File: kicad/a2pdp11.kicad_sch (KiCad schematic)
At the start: 21 parts, among them SW1 HALT, SW2 INIT, U1 74LS07, U2 DCJ11, U3 SN74LVC245AN, U4 SN74LVC245AN, U5 SN74LVC245AN, U6 SN74LVC245AN, U7 TangNano9K, U8 SN74LVC245AN, Y1 18M

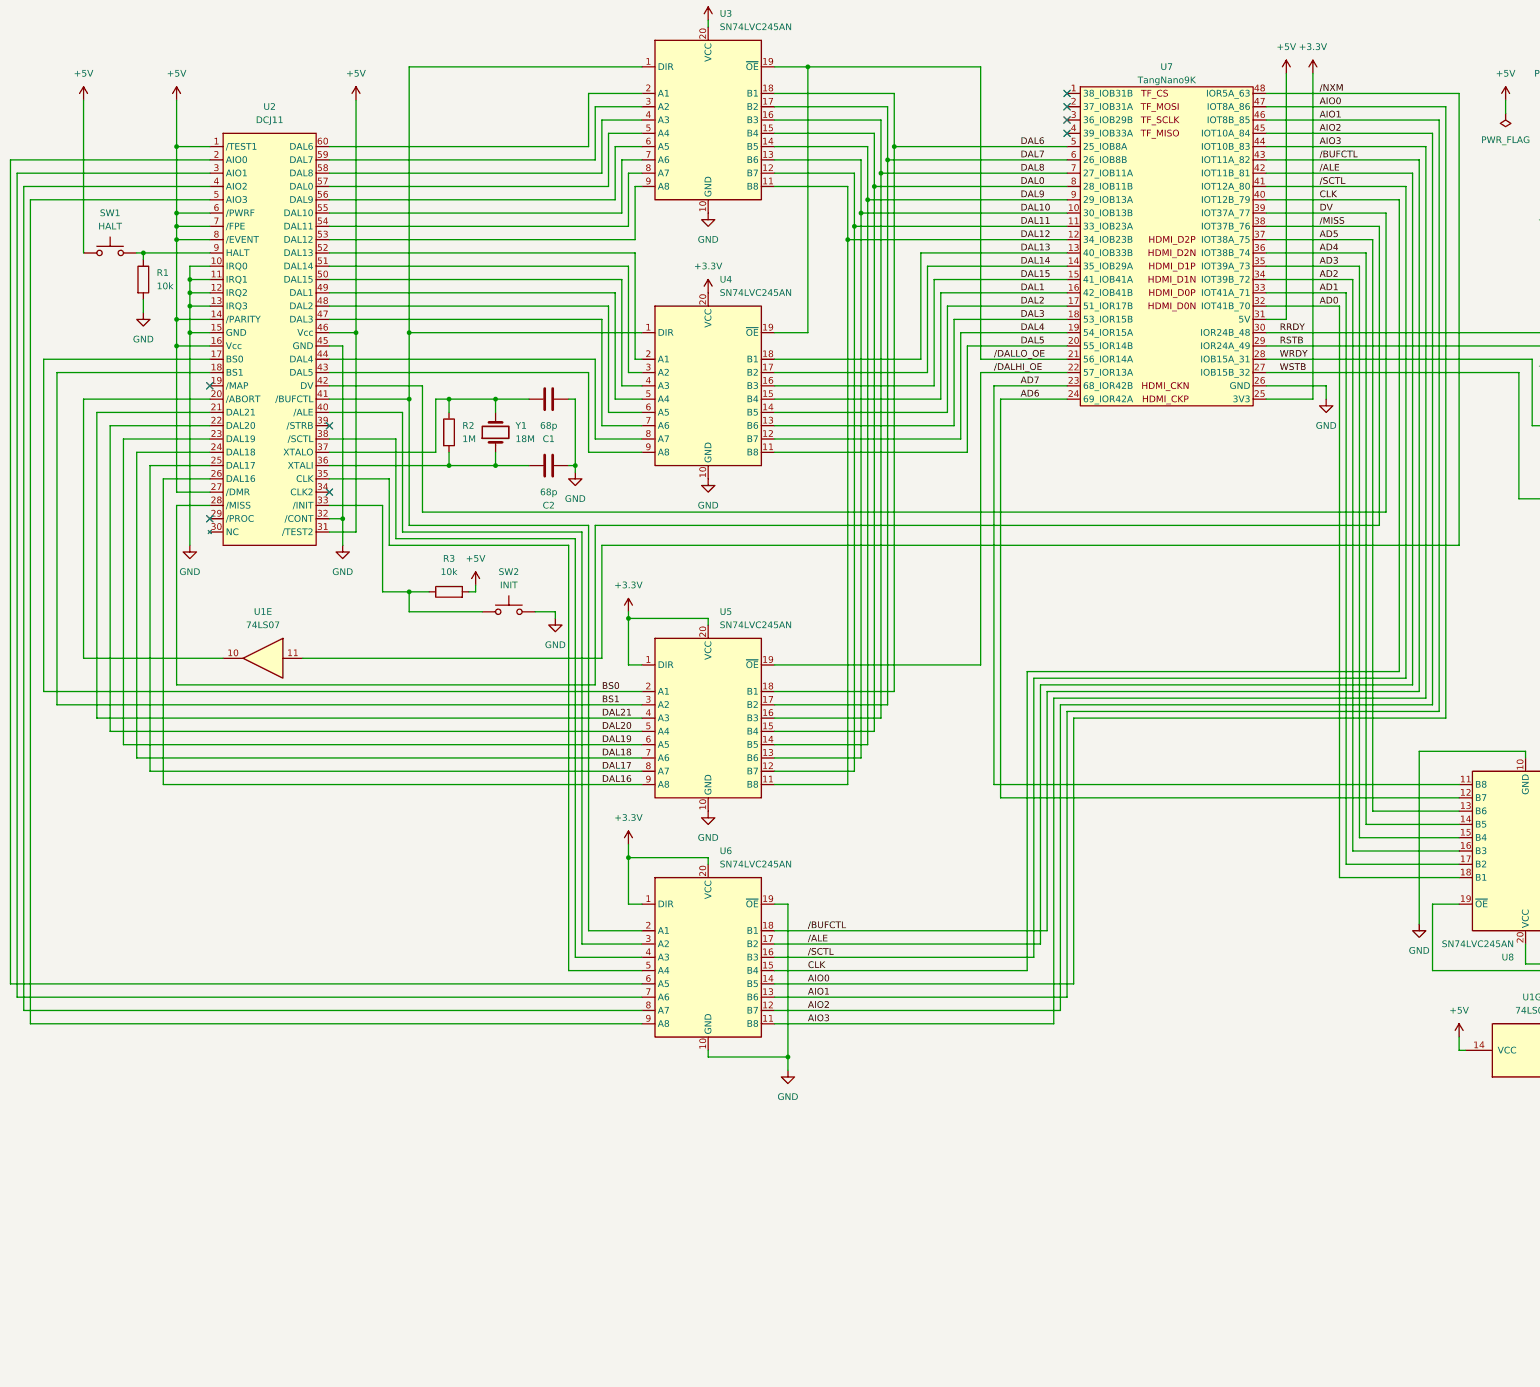
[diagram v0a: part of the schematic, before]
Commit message: aio multiplexed
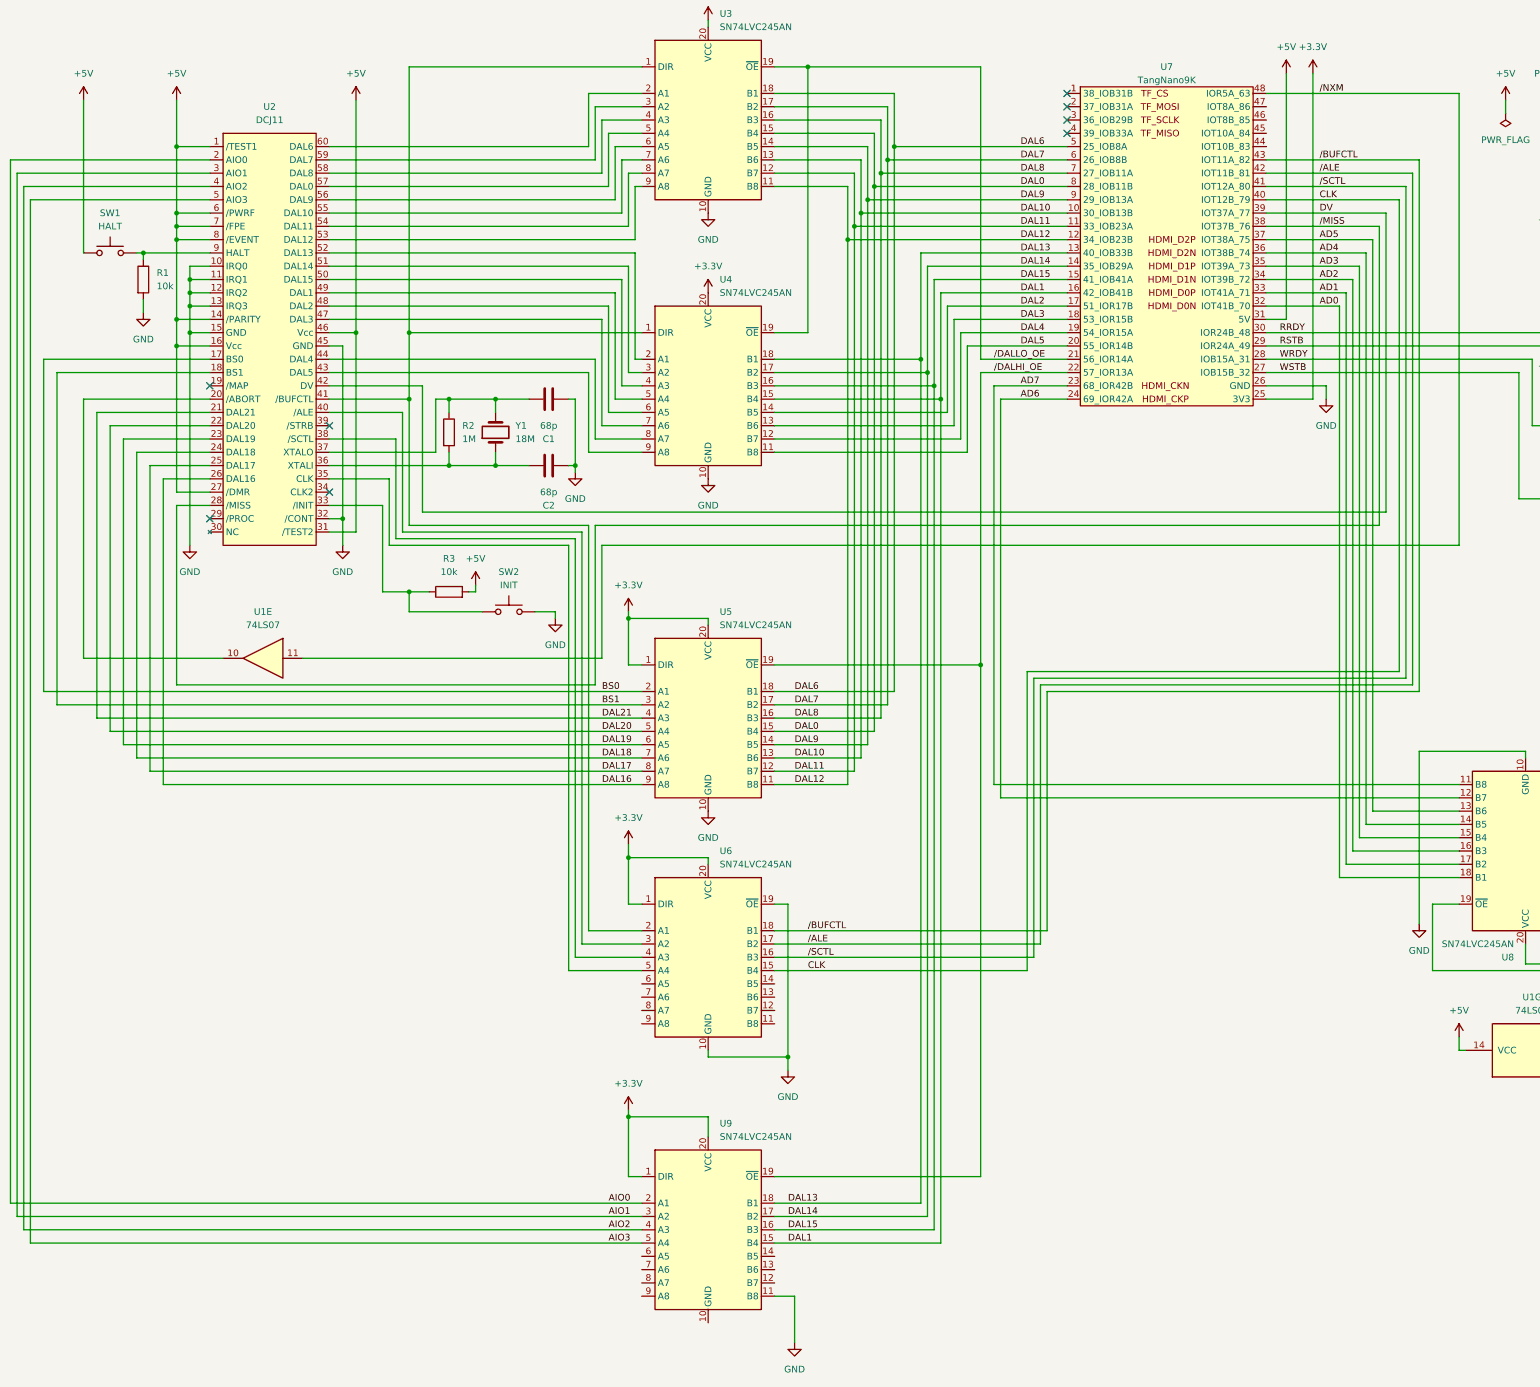
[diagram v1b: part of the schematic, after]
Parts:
- added U9: SN74LVC245AN, Package_DIP:DIP-20_W7.62mm, symbol Apple2_bus:SN74LVC245AN
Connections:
- net +3.3V: now also U9.1 (DIR), U9.20 (VCC)
- net AIO0: now also U2.2 (AIO0), U9.2 (A1); no longer U6.14 (B5), U7.47 (IOT8A_86)
- net AIO1: now also U2.3 (AIO1), U9.3 (A2); no longer U6.13 (B6), U7.46 (IOT8B_85)
- net AIO2: now also U2.4 (AIO2), U9.4 (A3); no longer U6.12 (B7), U7.45 (IOT10A_84)
- net AIO3: now also U2.5 (AIO3), U9.5 (A4); no longer U6.11 (B8), U7.44 (IOT10B_83)
- net DAL1: now also U9.15 (B4)
- net DAL13: now also U9.18 (B1)
- net DAL14: now also U9.17 (B2)
- net DAL15: now also U9.16 (B3)
- net GND: now also U9.11 (B8)
- net /DALHI_OE: now also U9.19 (~{OE})
- net at U6.6 (A5): no longer U2.2 (AIO0)
- net at U6.7 (A6): no longer U2.3 (AIO1)
- net at U6.8 (A7): no longer U2.4 (AIO2)
- net at U6.9 (A8): no longer U2.5 (AIO3)
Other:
- title: J11 Test 11 -> J11 Test 12

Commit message: dalhi_oe_n = !dalhi_oe_n
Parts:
- removed U1: 74LS07, symbol 74xx:74LS07
- added R8: 4.7k, symbol Apple2_bus:R
- added U1: 74LS00, symbol 74xx:74LS00
- added U10: 74LS05, symbol 74xx:74LS05
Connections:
- net +3.3V: now also R8.2
- net +5V: now also U10.14 (VCC)
- net GND: now also U10.7 (GND)
- net /DALLO_OE: now also U1.1, U1.2
- net at U2.20 (/ABORT): now also U10.2
- net at A1.16 (D13), R6.1: now also U10.10
- net at A1.20 (A1), R7.1: now also U10.8
- net at A1.15 (D12): now also U10.5
- net at A1.19 (A0): now also U10.3
- net RRDY renamed /RRDY
- net /RRDY: now also U10.6
- net RSTB renamed /RSTB
- net /RSTB: now also U10.11
- net WRDY renamed /WRDY
- net /WRDY: now also U10.4
- net WSTB renamed /WSTB
- net /WSTB: now also U10.9
- net /DALHI_OE: no longer names the net of U5.19 (~{OE}), U9.19 (~{OE})
- net /DALHI_OE: now also U1.3; no longer U7.22 (57_IOR13A)
- net /NXM renamed NXM
- net NXM: now also U10.1
- new net: R8.1, U10.12
- no-connect marks 24 -> 22
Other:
- title: J11 Test 12 -> J11 Test 13

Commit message: run BASIC, but unstable
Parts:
- removed R4, R5, R6, R7, R8: 4.7k, symbol Apple2_bus:R
- removed U10: 74LS05, symbol 74xx:74LS05
- added U11: AE-LCNV4-MOSFET, symbol Apple2_bus:AE-LCNV4-MOSFET
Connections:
- net /RRDY is gone; now on net /DEVSEL: U7.30 (IOR24B_48)
- net /WSTB is gone; now on net R/W: U7.27 (IOB15B_32)
- net +3.3V: now also U11.9 (LV)
- net +5V: now also U11.4 (HV); no longer U2.8 (/EVENT)
- net GND: now also U9.10 (GND), U11.10 (GND), U11.3 (GND)
- net A0: now reaches U6.11 (B8)
- net A0: now also U7.44 (IOT10B_83)
- net A1: now reaches U6.12 (B7)
- net A1: now also U7.45 (IOT10A_84)
- net A2: now reaches U6.13 (B6)
- net A2: now also U7.46 (IOT8B_85)
- net A3: now reaches U6.14 (B5)
- net A3: now also U7.47 (IOT8A_86)
- net at U6.6 (A5): now also A1.16 (D13)
- net at U6.7 (A6): now also A1.15 (D12)
- net at U6.8 (A7): now also A1.14 (D11)
- net at U6.9 (A8): now also A1.13 (D10)
- net at A1.20 (A1): now also U11.1 (HV1)
- net at U2.20 (/ABORT): now also U11.6 (HV4)
- net at A1.19 (A0): now also U11.2 (HV2)
- net at A1.10 (D7): now also U8.13 (B6); no longer U8.4 (A3)
- net at A1.11 (D8): now also U8.12 (B7); no longer U8.3 (A2)
- net at A1.12 (D9): now also U8.11 (B8); no longer U8.2 (A1)
- net R/W: now reaches U8.1 (DIR)
- net R/W: now also U11.12 (LV1); no longer A1.13 (D10)
- net /DEVSEL: now reaches U8.19 (~{OE})
- net /DEVSEL: now also U11.11 (LV2); no longer A1.14 (D11)
- net at A1.5 (D2): now also U8.18 (B1); no longer U8.9 (A8)
- net at A1.6 (D3): now also U8.17 (B2); no longer U8.8 (A7)
- net at A1.7 (D4): now also U8.16 (B3); no longer U8.7 (A6)
- net at A1.8 (D5): now also U8.15 (B4); no longer U8.6 (A5)
- net at A1.9 (D6): now also U8.14 (B5); no longer U8.5 (A4)
- net /EVENT: now reaches U7.22 (57_IOR13A)
- net /EVENT: now also U2.8 (/EVENT)
- net AD0 renamed D2
- net D2: now also U8.4 (A3); no longer U8.18 (B1)
- net AD1 renamed D3
- net D3: now also U8.5 (A4); no longer U8.17 (B2)
- net AD2 renamed D4
- net D4: now also U8.6 (A5); no longer U8.16 (B3)
- net AD3 renamed D5
- net D5: now also U8.7 (A6); no longer U8.15 (B4)
- net AD4 renamed D6
- net D6: now also U8.8 (A7); no longer U8.14 (B5)
- net AD5 renamed D7
- net D7: now also U8.9 (A8); no longer U8.13 (B6)
- net AD6 renamed D0
- net D0: now also U8.2 (A1); no longer U8.12 (B7)
- net AD7 renamed D1
- net D1: now also U8.3 (A2); no longer U8.11 (B8)
- net NXM renamed /NXM
- net /NXM: now also U11.7 (LV4)
- net /RSTB: no longer names the net of U7.29 (IOR24A_49)
- net /WRDY: no longer names the net of U7.28 (IOB15A_31)
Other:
- title: J11 Test 13 -> J11 Test 14
- moved on the sheet: U1A, U1B, U1C, U1D, U8, U9

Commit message: Apple II interface
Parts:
- removed A1: Arduino_Nano_v3.x, Module:Arduino_Nano, symbol MCU_Module:Arduino_Nano_v3.x
- removed R1: 10k, symbol Apple2_bus:R
- added A1BUS1: A2_BUS, Apple2_bus:BUS_A2, symbol Apple2_bus:A2_BUS
- added C10, C13, C5, C6, C7, C8, C9: 0.1u, Apple2_bus:C_Disc_D4.3mm_W1.9mm_P5.08mm, symbol Device:C
- added C11, C12: 10u, Apple2_bus:CP_Radial_D5.0mm_P2.00mm, symbol Apple2_bus:C_Polarized
- added C3, C4: 0.33u, Apple2_bus:C_Disc_D4.3mm_W1.9mm_P5.08mm, symbol Device:C
- added D1: 1N4001, Diode_THT:D_DO-41_SOD81_P10.16mm_Horizontal, symbol Diode:1N4001
- added J1: DCJ11A, Connector_PinHeader_2.54mm:PinHeader_1x30_P2.54mm_Vertical, symbol Connector_Generic:Conn_01x30
- added J10: ~, Connector_PinSocket_2.54mm:PinSocket_2x03_P2.54mm_Vertical, symbol Connector_Generic:Conn_02x03_Odd_Even
- added J2: DCJ11B, Connector_PinHeader_2.54mm:PinHeader_1x30_P2.54mm_Vertical, symbol Connector_Generic:Conn_01x30
- added J3, J4: TN9A, Connector_PinHeader_2.54mm:PinHeader_1x24_P2.54mm_Vertical, symbol Connector_Generic:Conn_01x24
- added J5: A2BUSA, Connector_PinHeader_2.54mm:PinHeader_1x25_P2.54mm_Vertical, symbol Connector_Generic:Conn_01x25
- added J6: A2BUSB, Connector_PinHeader_2.54mm:PinHeader_1x25_P2.54mm_Vertical, symbol Connector_Generic:Conn_01x25
- added J7: 3V3, Connector_PinHeader_2.54mm:PinHeader_1x02_P2.54mm_Vertical, symbol Connector:Conn_01x02_Pin
- added J8: 5V, Connector_PinHeader_2.54mm:PinHeader_1x02_P2.54mm_Vertical, symbol Connector:Conn_01x02_Pin
- added J9: Jumper, Connector_PinHeader_2.54mm:PinHeader_2x09_P2.54mm_Vertical, symbol Connector_Generic:Conn_02x09_Odd_Even
- added JP1: RES-INIT, Connector_PinHeader_2.54mm:PinHeader_2x01_P2.54mm_Vertical, symbol Jumper:Jumper_2_Open
- added JP2: IOSEL-HALT, Connector_PinHeader_2.54mm:PinHeader_2x01_P2.54mm_Vertical, symbol Jumper:Jumper_2_Open
- added R2, R3, R5: 10k, Resistor_THT:R_Axial_DIN0207_L6.3mm_D2.5mm_P10.16mm_Horizontal, symbol Apple2_bus:R
- C1, C2: footprint (none) -> Apple2_bus:C_Disc_D3.0mm_W1.6mm_P2.54mm
- R1: renamed from R2; footprint (none) -> Resistor_THT:R_Axial_DIN0207_L6.3mm_D2.5mm_P10.16mm_Horizontal
- R4: renamed from R3; footprint (none) -> Resistor_THT:R_Axial_DIN0207_L6.3mm_D2.5mm_P10.16mm_Horizontal
- SW1, SW2: footprint (none) -> Button_Switch_THT:SW_PUSH_6mm_H4.3mm
- U1: renamed from U2; footprint DCJ11 -> Apple2_bus:DCJ11
- U11: footprint (none) -> Apple2_bus:AE-LCNV4-MOSFET
- U8: renamed from U7; footprint (none) -> Apple2_bus:TangNano9K
- U9: renamed from U1; footprint (none) -> Apple2_bus:DIP-14_W7.62mm_Socket
- Y1: footprint (none) -> Crystal:Crystal_HC18-U_Horizontal
- renumbered U3 to U2, U4 to U3, U5 to U4, U9 to U5, U8 to U7
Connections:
- net +3.3V: now also C10.1, C11.1, C5.1, C6.1, C7.1, C8.1, C9.1, J4.24 (Pin_24), J7.2 (Pin_2)
- net +5V: now also U9.14 (VCC), A1BUS1.25 (+5V), C12.1, C13.1, C3.1, C4.1, D1.2 (A), J1.16 (Pin_16), J2.15 (Pin_15), J6.1 (Pin_1), J8.2 (Pin_2), J9.10 (Pin_10), J9.16 (Pin_16), J9.18 (Pin_18), J9.2 (Pin_2), J9.4 (Pin_4), J9.6 (Pin_6), J9.8 (Pin_8), R2.2, R3.2, R5.2; no longer SW1.1, U1.1 (/TEST1), U1.14 (/PARITY), U1.27 (/DMR), U1.31 (/TEST2), U1.6 (/PWRF), U1.7 (/FPE), U8.31 (5V)
- net A0: now also U6.14 (B5), J4.5 (Pin_5); no longer U6.11 (B8)
- net A1: now also U6.13 (B6), J4.4 (Pin_4); no longer U6.12 (B7)
- net A2: now also U6.12 (B7), J4.3 (Pin_3); no longer U6.13 (B6)
- net A3: now also U6.11 (B8), J4.2 (Pin_2); no longer U6.14 (B5)
- net AIO0: now also J1.2 (Pin_2)
- net AIO1: now also J1.3 (Pin_3)
- net AIO2: now also J1.4 (Pin_4)
- net AIO3: now also J1.5 (Pin_5)
- net BS0: now also J1.17 (Pin_17)
- net BS1: now also J1.18 (Pin_18)
- net CLK: now also U8.41 (IOT12A_80), J4.8 (Pin_8); no longer U8.40 (IOT12B_79)
- net D0: now also J3.24 (Pin_24)
- net D1: now also J3.23 (Pin_23)
- net D2: now also J4.17 (Pin_17)
- net D3: now also J4.16 (Pin_16)
- net D4: now also J4.15 (Pin_15)
- net D5: now also J4.14 (Pin_14)
- net D6: now also J4.13 (Pin_13)
- net D7: now also J4.12 (Pin_12)
- net DAL0: now also J3.8 (Pin_8)
- net DAL1: now also J3.16 (Pin_16)
- net DAL10: now also J3.10 (Pin_10)
- net DAL11: now also J3.11 (Pin_11)
- net DAL12: now also J3.12 (Pin_12)
- net DAL13: now also J3.13 (Pin_13)
- net DAL14: now also J3.14 (Pin_14)
- net DAL15: now also J3.15 (Pin_15)
- net DAL16: now also J1.26 (Pin_26)
- net DAL17: now also J1.25 (Pin_25)
- net DAL18: now also J1.24 (Pin_24)
- net DAL19: now also J1.23 (Pin_23)
- net DAL2: now also U5.14 (B5), J3.17 (Pin_17)
- net DAL20: now also J1.22 (Pin_22)
- net DAL21: now also J1.21 (Pin_21)
- net DAL3: now also J3.18 (Pin_18)
- net DAL4: now also J3.19 (Pin_19)
- net DAL5: now also J3.20 (Pin_20)
- net DAL6: now also J3.5 (Pin_5)
- net DAL7: now also J3.6 (Pin_6)
- net DAL8: now also J3.7 (Pin_7)
- net DAL9: now also J3.9 (Pin_9)
- net DV: now also J2.19 (Pin_19), J9.15 (Pin_15); no longer U8.39 (IOT37A_77)
- net GND: now also SW1.2, U9.7 (GND), A1BUS1.26 (GND), C10.2, C11.2, C12.2, C13.2, C3.2, C4.2, C5.2, C6.2, C7.2, C8.2, C9.2, J1.15 (Pin_15), J2.16 (Pin_16), J4.23 (Pin_23), J5.1 (Pin_1), J9.12 (Pin_12), J9.14 (Pin_14); no longer U1.10 (IRQ0), U1.11 (IRQ1), U1.12 (IRQ2), U1.13 (IRQ3), U1.32 (/CONT), U5.11 (B8)
- net IRQ0: now also U1.11 (IRQ1), U8.30 (IOR24B_48), J1.11 (Pin_11), J4.19 (Pin_19)
- net IRQ1: now also U1.10 (IRQ0), U8.29 (IOR24A_49), J1.10 (Pin_10), J4.20 (Pin_20)
- net R/W: now also J4.22 (Pin_22)
- net /ALE: now also J4.7 (Pin_7)
- net /BUFCTL: now also J4.6 (Pin_6)
- net /DALLO_OE: now also J3.21 (Pin_21)
- net /DEVSEL: now also U8.28 (IOB15A_31), J4.21 (Pin_21); no longer U8.30 (IOR24B_48)
- net /EVENT: now also J1.8 (Pin_8), J3.22 (Pin_22)
- net /MISS: now also J1.28 (Pin_28), J4.11 (Pin_11)
- net /NXM: now also J4.1 (Pin_1)
- net /SCTL: now also U8.40 (IOT12B_79), J4.9 (Pin_9); no longer U8.41 (IOT12A_80)
- net at U1.41 (/BUFCTL), U2.1 (DIR), U3.1 (DIR)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: now also J2.20 (Pin_20)
- net at U1.40 (/ALE), U6.3 (A2): now also J2.21 (Pin_21)
- net at U1.38 (/SCTL), U6.4 (A3): now also J2.23 (Pin_23)
- net at U1.35 (CLK), U6.5 (A4): now also J2.26 (Pin_26)
- net at U6.6 (A5): now also A1BUS1.2 (A0), J6.24 (Pin_24)
- net at U6.7 (A6): now also A1BUS1.3 (A1), J6.23 (Pin_23)
- net at U6.8 (A7): now also A1BUS1.4 (A2), J6.22 (Pin_22)
- net at U6.9 (A8): now also A1BUS1.5 (A3), J6.21 (Pin_21)
- net at U9.11: now also U1.33 (/INIT), J2.28 (Pin_28)
- net at U9.12: now also U9.13, U9.8
- net at U9.10: now also JP1.1 (A), R5.1
- net at U9.9: now also R4.1, SW2.1
- net at C2.1, R1.2, Y1.1: now also U1.37 (XTALO), J2.24 (Pin_24); no longer U1.36 (XTALI)
- net at C1.1, R1.1, Y1.2: now also U1.36 (XTALI), J2.25 (Pin_25); no longer U1.37 (XTALO)
- net MAP: now reaches U1.19 (/MAP)
- net MAP: now also U5.6 (A5), J1.19 (Pin_19)
- net at U1.20 (/ABORT), U11.6 (HV4): now also J1.20 (Pin_20)
- net at U1.29 (/PROC): now also J1.29 (Pin_29)
- net at U1.30 (NC): now also J1.30 (Pin_30)
- net at U1.34 (CLK2): now also J2.27 (Pin_27)
- net at U1.39 (/STRB): now also J2.22 (Pin_22)
- net at U1.43 (DAL5), U3.9 (A8): now also J2.18 (Pin_18)
- net at U1.44 (DAL4), U3.8 (A7): now also J2.17 (Pin_17)
- net at U1.47 (DAL3), U3.7 (A6): now also J2.14 (Pin_14)
- net at U1.48 (DAL2), U3.6 (A5): now also J2.13 (Pin_13)
- net at U1.49 (DAL1), U3.5 (A4): now also J2.12 (Pin_12)
- net at U1.50 (DAL15), U3.4 (A3): now also J2.11 (Pin_11)
- net at U1.51 (DAL14), U3.3 (A2): now also J2.10 (Pin_10)
- net at U1.52 (DAL13), U3.2 (A1): now also J2.9 (Pin_9)
- net at U1.53 (DAL12), U2.9 (A8): now also J2.8 (Pin_8)
- net at U1.54 (DAL11), U2.8 (A7): now also J2.7 (Pin_7)
- net at U1.55 (DAL10), U2.7 (A6): now also J2.6 (Pin_6)
- net at U1.56 (DAL9), U2.6 (A5): now also J2.5 (Pin_5)
- net at U1.57 (DAL0), U2.5 (A4): now also J2.4 (Pin_4)
- net at U1.58 (DAL8), U2.4 (A3): now also J2.3 (Pin_3)
- net at U1.59 (DAL7), U2.3 (A2): now also J2.2 (Pin_2)
- net at U1.60 (DAL6), U2.2 (A1): now also J2.1 (Pin_1)
- net at U1.9 (HALT): now also U9.6, J1.9 (Pin_9); no longer SW1.2
- net at U5.12 (B7): now also J10.4 (Pin_4)
- net at U5.13 (B6): now also J10.2 (Pin_2)
- net at U5.7 (A6): now also J10.1 (Pin_1)
- net at U5.8 (A7): now also J10.3 (Pin_3)
- net at U5.9 (A8): now also J10.5 (Pin_5)
- net at U7.13 (B6): now also A1BUS1.44 (D5), J5.19 (Pin_19)
- net at U7.12 (B7): now also A1BUS1.43 (D6), J5.18 (Pin_18)
- net at U7.11 (B8): now also A1BUS1.42 (D7), J5.17 (Pin_17)
- net at U11.2 (HV2): now also A1BUS1.41 (~{DEVSEL}), J5.16 (Pin_16)
- net at U11.1 (HV1): now also A1BUS1.18 (R/~{W}), J6.8 (Pin_8)
- net at U7.18 (B1): now also A1BUS1.49 (D0), J5.24 (Pin_24)
- net at U7.17 (B2): now also A1BUS1.48 (D1), J5.23 (Pin_23)
- net at U7.16 (B3): now also A1BUS1.47 (D2), J5.22 (Pin_22)
- net at U7.15 (B4): now also A1BUS1.46 (D3), J5.21 (Pin_21)
- net at U7.14 (B5): now also A1BUS1.45 (D4), J5.20 (Pin_20)
- net at U11.5 (HV3): now also J8.1 (Pin_1)
- net at U11.8 (LV3): now also J7.1 (Pin_1)
- net at U9.4: now also SW1.1, R2.1
- net at U9.5: now also JP2.1 (A), R3.1
- net at U8.1 (38_IOB31B): now also J3.1 (Pin_1)
- net at U8.2 (37_IOB31A): now also J3.2 (Pin_2)
- net at U8.3 (36_IOB29B): now also J3.3 (Pin_3)
- net at U8.4 (39_IOB33A): now also J3.4 (Pin_4)
- new net: A1BUS1.1 (~{I/O_SEL}), J6.25 (Pin_25), JP2.2 (B)
- new net: A1BUS1.10 (A8), J6.16 (Pin_16)
- new net: A1BUS1.11 (A9), J6.15 (Pin_15)
- new net: A1BUS1.12 (A10), J6.14 (Pin_14)
- new net: A1BUS1.13 (A11), J6.13 (Pin_13)
- new net: A1BUS1.14 (A12), J6.12 (Pin_12)
- new net: A1BUS1.15 (A13), J6.11 (Pin_11)
- new net: A1BUS1.16 (A14), J6.10 (Pin_10)
- new net: A1BUS1.17 (A15), J6.9 (Pin_9)
- new net: A1BUS1.19 (~{SYNC}), J6.7 (Pin_7)
- new net: A1BUS1.20 (~{STROBE}), J6.6 (Pin_6)
- new net: A1BUS1.21 (RDY), J6.5 (Pin_5)
- new net: A1BUS1.22 (~{DMA}), J6.4 (Pin_4)
- new net: A1BUS1.23 (INT_OUT), A1BUS1.28 (INT_IN), J5.3 (Pin_3), J6.3 (Pin_3)
- new net: A1BUS1.24 (DMA_OUT), A1BUS1.27 (DMA_IN), J5.2 (Pin_2), J6.2 (Pin_2)
- new net: A1BUS1.29 (~{NMI}), J5.4 (Pin_4)
- new net: A1BUS1.30 (~{IRQ}), J5.5 (Pin_5)
- new net: A1BUS1.31 (~{RES}), J5.6 (Pin_6), JP1.2 (B)
- new net: A1BUS1.32 (~{INH}), J5.7 (Pin_7)
- new net: A1BUS1.33 (-12V), J5.8 (Pin_8)
- new net: A1BUS1.34 (-5V), J5.9 (Pin_9)
- new net: A1BUS1.35 (COLREF), J5.10 (Pin_10)
- new net: A1BUS1.36 (7M), J5.11 (Pin_11)
- new net: A1BUS1.37 (Q3), J5.12 (Pin_12)
- new net: A1BUS1.38 (ø1), J5.13 (Pin_13)
- new net: A1BUS1.39 (~{M2SEL}), J5.14 (Pin_14)
- new net: A1BUS1.40 (ø0), J5.15 (Pin_15)
- new net: A1BUS1.50 (+12V), J5.25 (Pin_25)
- new net: A1BUS1.6 (A4), J6.20 (Pin_20)
- new net: A1BUS1.7 (A5), J6.19 (Pin_19)
- new net: A1BUS1.8 (A6), J6.18 (Pin_18)
- new net: A1BUS1.9 (A7), J6.17 (Pin_17)
- new net: D1.1 (K), J4.18 (Pin_18), U8.31 (5V)
- new net: J10.6 (Pin_6), U5.11 (B8)
- new net IRQ2: J1.12 (Pin_12), J9.11 (Pin_11), U1.12 (IRQ2)
- new net IRQ3: J1.13 (Pin_13), J9.13 (Pin_13), U1.13 (IRQ3)
- new net /CONT: J2.29 (Pin_29), J4.10 (Pin_10), U1.32 (/CONT), U8.39 (IOT37A_77)
- new net /DMR: J1.27 (Pin_27), J9.9 (Pin_9), U1.27 (/DMR)
- new net /FPE: J1.7 (Pin_7), J9.5 (Pin_5), U1.7 (/FPE)
- new net /PARITY: J1.14 (Pin_14), J9.7 (Pin_7), U1.14 (/PARITY)
- new net /PWRF: J1.6 (Pin_6), J9.3 (Pin_3), U1.6 (/PWRF)
- new net /TEST1: J1.1 (Pin_1), J9.1 (Pin_1), U1.1 (/TEST1)
- new net /TEST2: J2.30 (Pin_30), J9.17 (Pin_17), U1.31 (/TEST2)
- no-connect marks 22 -> 0
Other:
- title: J11 Test 14 -> J11 Test 15
- moved on the sheet: C1, C2, R1, R4, SW2, U11, U2, U3, U4, U5, U6, U7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

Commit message: Apple II Interface
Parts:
- removed J10: ~, Connector_PinSocket_2.54mm:PinSocket_2x03_P2.54mm_Vertical, symbol Connector_Generic:Conn_02x03_Odd_Even
- renumbered A1BUS1 to A2BUS1
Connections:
- net A0: now also A2BUS1.2 (A0), J6.24 (Pin_24), U5.9 (A8); no longer J4.5 (Pin_5), U6.14 (B5), U8.44 (IOT10B_83)
- net A1: now also A2BUS1.3 (A1), J6.23 (Pin_23), U5.8 (A7); no longer J4.4 (Pin_4), U6.13 (B6), U8.45 (IOT10A_84)
- net A2: now also A2BUS1.4 (A2), J6.22 (Pin_22), U5.7 (A6); no longer J4.3 (Pin_3), U6.12 (B7), U8.46 (IOT8B_85)
- net A3: now also A2BUS1.5 (A3), J6.21 (Pin_21), U5.6 (A5); no longer J4.2 (Pin_2), U6.11 (B8), U8.47 (IOT8A_86)
- net AIO0: now also J4.2 (Pin_2), U6.11 (B8), U8.47 (IOT8A_86); no longer J1.2 (Pin_2), U1.2 (AIO0), U5.2 (A1)
- net AIO1: now also J4.3 (Pin_3), U6.12 (B7), U8.46 (IOT8B_85); no longer J1.3 (Pin_3), U1.3 (AIO1), U5.3 (A2)
- net AIO2: now also J4.4 (Pin_4), U6.13 (B6), U8.45 (IOT10A_84); no longer J1.4 (Pin_4), U1.4 (AIO2), U5.4 (A3)
- net AIO3: now also J4.5 (Pin_5), U6.14 (B5), U8.44 (IOT10B_83); no longer J1.5 (Pin_5), U1.5 (AIO3), U5.5 (A4)
- net DAL3: now also U5.13 (B6)
- net DAL4: now also U5.12 (B7)
- net DAL5: now also U5.11 (B8)
- net at A2BUS1.1 (~{I/O_SEL}), J6.25 (Pin_25): now also U11.2 (HV2); no longer JP2.2 (B)
- net at A2BUS1.41 (~{DEVSEL}), J5.16 (Pin_16): now also JP2.2 (B); no longer U11.2 (HV2)
- net A4: now reaches A2BUS1.6 (A4), J6.20 (Pin_20)
- net A4: now also U5.5 (A4)
- net A5: now reaches A2BUS1.7 (A5), J6.19 (Pin_19)
- net A5: now also U5.4 (A3)
- net A6: now reaches A2BUS1.8 (A6), J6.18 (Pin_18)
- net A6: now also U5.3 (A2)
- net A7: now reaches A2BUS1.9 (A7), J6.17 (Pin_17)
- net A7: now also U5.2 (A1)
- net MAP: no longer names the net of J1.19 (Pin_19), U1.19 (/MAP)
- net MAP: no longer U5.6 (A5)
- new net: J1.5 (Pin_5), U1.5 (AIO3), U6.6 (A5)
- new net: J1.4 (Pin_4), U1.4 (AIO2), U6.7 (A6)
- new net: J1.3 (Pin_3), U1.3 (AIO1), U6.8 (A7)
- new net: J1.2 (Pin_2), U1.2 (AIO0), U6.9 (A8)
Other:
- title: J11 Test 15 -> J11 Test 16
- moved on the sheet: JP1, JP2, U5, U6
